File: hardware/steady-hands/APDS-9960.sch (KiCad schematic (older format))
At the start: 8 parts

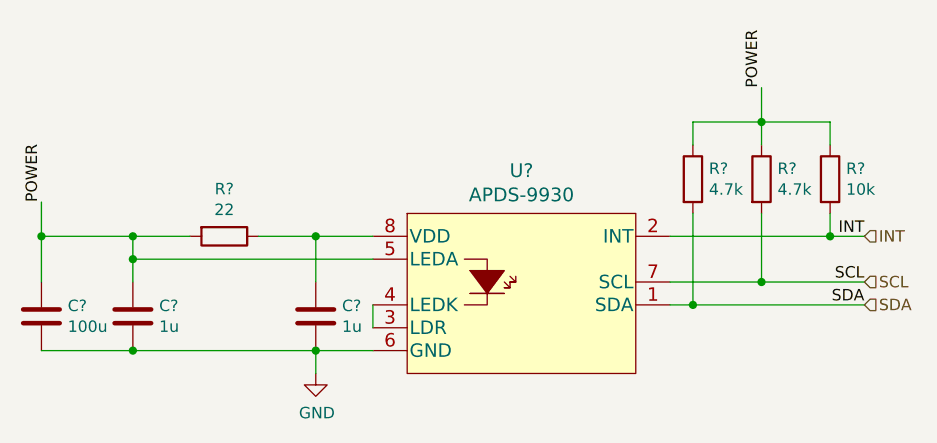
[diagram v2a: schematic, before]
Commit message: Completes schematic connections
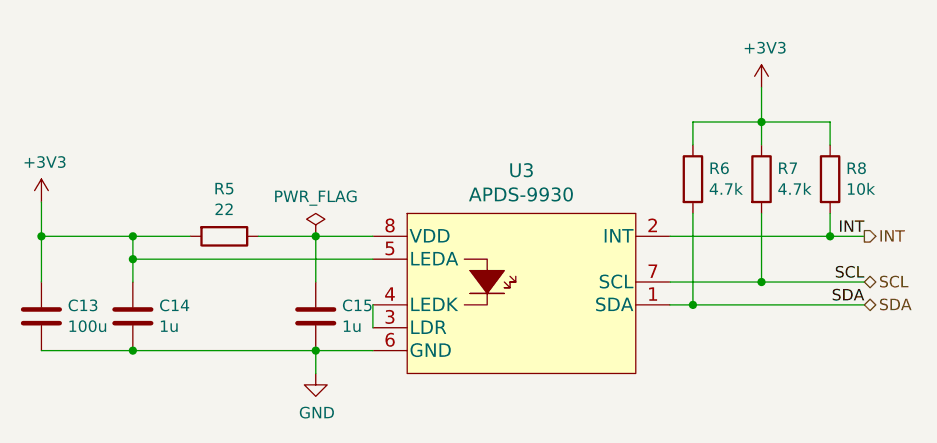
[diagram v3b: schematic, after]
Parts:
- gave numbers to parts that had none: 8
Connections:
- net POWER renamed +3V3
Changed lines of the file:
@@
 $Descr A4 11693 8268
 encoding utf-8
-Sheet 3 7
+Sheet 2 7
 Title ""
 Date ""
@@
 P 6050 3600
 AR Path="/5EF9057A" Ref="U?"  Part="1"
-AR Path="/5EF838FE/5EF9057A" Ref="U?"  Part="1"
-F 0 "U?" H 6050 3787 60  0000 C CNN
+AR Path="/5EF838FE/5EF9057A" Ref="U3"  Part="1"
+F 0 "U3" H 6050 3787 60  0000 C CNN
 F 1 "APDS-9930" H 6050 3681 60  0000 C CNN
 F 2 "QFN_DS-9930" H 6050 3600 60  0001 C CNN
@@
 P 4350 4050
 AR Path="/5EF90580" Ref="C?"  Part="1"
-AR Path="/5EF838FE/5EF90580" Ref="C?"  Part="1"
-F 0 "C?" H 4235 4004 50  0000 R CNN
+AR Path="/5EF838FE/5EF90580" Ref="C14"  Part="1"
+F 0 "C14" H 4235 4004 50  0000 R CNN
 F 1 "1u" H 4235 4095 50  0000 R CNN
 F 2 "" H 4388 3900 50  0001 C CNN
@@
 P 5150 4050
 AR Path="/5EF90586" Ref="C?"  Part="1"
-AR Path="/5EF838FE/5EF90586" Ref="C?"  Part="1"
-F 0 "C?" H 5035 4004 50  0000 R CNN
+AR Path="/5EF838FE/5EF90586" Ref="C15"  Part="1"
+F 0 "C15" H 5035 4004 50  0000 R CNN
 F 1 "1u" H 5035 4095 50  0000 R CNN
 F 2 "" H 5188 3900 50  0001 C CNN
@@
 P 5150 4300
 AR Path="/5EF9058C" Ref="#PWR?"  Part="1"
-AR Path="/5EF838FE/5EF9058C" Ref="#PWR?"  Part="1"
-F 0 "#PWR?" H 5150 4050 50  0001 C CNN
+AR Path="/5EF838FE/5EF9058C" Ref="#PWR0125"  Part="1"
+F 0 "#PWR0125" H 5150 4050 50  0001 C CNN
 F 1 "GND" H 5155 4127 50  0000 C CNN
 F 2 "" H 5150 4300 50  0001 C CNN
@@
 P 4750 3700
 AR Path="/5EF90592" Ref="R?"  Part="1"
-AR Path="/5EF838FE/5EF90592" Ref="R?"  Part="1"
-F 0 "R?" V 4543 3700 50  0000 C CNN
+AR Path="/5EF838FE/5EF90592" Ref="R5"  Part="1"
+F 0 "R5" V 4543 3700 50  0000 C CNN
 F 1 "22" V 4634 3700 50  0000 C CNN
 F 2 "" V 4680 3700 50  0001 C CNN
@@
 P 3950 4050
 AR Path="/5EF905A6" Ref="C?"  Part="1"
-AR Path="/5EF838FE/5EF905A6" Ref="C?"  Part="1"
-F 0 "C?" H 3835 4004 50  0000 R CNN
+AR Path="/5EF838FE/5EF905A6" Ref="C13"  Part="1"
+F 0 "C13" H 3835 4004 50  0000 R CNN
 F 1 "100u" H 3835 4095 50  0000 R CNN
 F 2 "" H 3988 3900 50  0001 C CNN
@@
 P 6800 3450
 AR Path="/5EF905AE" Ref="R?"  Part="1"
-AR Path="/5EF838FE/5EF905AE" Ref="R?"  Part="1"
-F 0 "R?" H 6870 3496 50  0000 L CNN
+AR Path="/5EF838FE/5EF905AE" Ref="R6"  Part="1"
+F 0 "R6" H 6870 3496 50  0000 L CNN
 F 1 "4.7k" H 6870 3405 50  0000 L CNN
 F 2 "" V 6730 3450 50  0001 C CNN
@@
 P 7100 3450
 AR Path="/5EF905B4" Ref="R?"  Part="1"
-AR Path="/5EF838FE/5EF905B4" Ref="R?"  Part="1"
-F 0 "R?" H 7170 3496 50  0000 L CNN
+AR Path="/5EF838FE/5EF905B4" Ref="R7"  Part="1"
+F 0 "R7" H 7170 3496 50  0000 L CNN
 F 1 "4.7k" H 7170 3405 50  0000 L CNN
 F 2 "" V 7030 3450 50  0001 C CNN
@@
 P 7400 3450
 AR Path="/5EF905BA" Ref="R?"  Part="1"
-AR Path="/5EF838FE/5EF905BA" Ref="R?"  Part="1"
-F 0 "R?" H 7470 3496 50  0000 L CNN
+AR Path="/5EF838FE/5EF905BA" Ref="R8"  Part="1"
+F 0 "R8" H 7470 3496 50  0000 L CNN
 F 1 "10k" H 7470 3405 50  0000 L CNN
 F 2 "" V 7330 3450 50  0001 C CNN
@@
 Wire Wire Line
 	3950 4200 4350 4200
-Text Label 3950 3550 1    50   ~ 0
-POWER
-Text Label 7100 3050 1    50   ~ 0
-POWER
 Text Label 7550 3700 2    50   ~ 0
 INT
@@
 Text Label 7550 4000 2    50   ~ 0
 SDA
-Text HLabel 7550 3700 2    50   Input ~ 0
+Text HLabel 7550 3700 2    50   Output ~ 0
 INT
-Text HLabel 7550 3900 2    50   Input ~ 0
+Text HLabel 7550 3900 2    50   BiDi ~ 0
 SCL
-Text HLabel 7550 4000 2    50   Input ~ 0
+Text HLabel 7550 4000 2    50   BiDi ~ 0
 SDA
+$Comp
+L power:+3V3 #PWR0164
+U 1 1 5F25AE43
+P 7100 3050
+F 0 "#PWR0164" H 7100 2900 50  0001 C CNN
+F 1 "+3V3" H 7115 3223 50  0000 C CNN
+F 2 "" H 7100 3050 50  0001 C CNN
+F 3 "" H 7100 3050 50  0001 C CNN
+	1    7100 3050
+	1    0    0    -1
+$EndComp
+$Comp
+L power:+3V3 #PWR0165
+U 1 1 5F25AF93
+P 3950 3550
+F 0 "#PWR0165" H 3950 3400 50  0001 C CNN
+F 1 "+3V3" H 3965 3723 50  0000 C CNN
+F 2 "" H 3950 3550 50  0001 C CNN
+F 3 "" H 3950 3550 50  0001 C CNN
+	1    3950 3550
+	1    0    0    -1
+$EndComp
+$Comp
+L power:PWR_FLAG #FLG0109
+U 1 1 5F25B62C
+P 5150 3700
+F 0 "#FLG0109" H 5150 3775 50  0001 C CNN
+F 1 "PWR_FLAG" H 5150 3873 50  0000 C CNN
+F 2 "" H 5150 3700 50  0001 C CNN
+F 3 "~" H 5150 3700 50  0001 C CNN
+	1    5150 3700
+	1    0    0    -1
+$EndComp
 $EndSCHEMATC

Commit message: Adds footprints
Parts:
- C13, C14, C15: footprint (none) -> Capacitor_SMD:C_0402_1005Metric
- R5, R6, R7, R8: footprint (none) -> Resistor_SMD:R_0402_1005Metric
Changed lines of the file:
@@
 F 0 "C14" H 4235 4004 50  0000 R CNN
 F 1 "1u" H 4235 4095 50  0000 R CNN
-F 2 "" H 4388 3900 50  0001 C CNN
+F 2 "Capacitor_SMD:C_0402_1005Metric" H 4388 3900 50  0001 C CNN
 F 3 "~" H 4350 4050 50  0001 C CNN
 	1    4350 4050
@@
 F 0 "C15" H 5035 4004 50  0000 R CNN
 F 1 "1u" H 5035 4095 50  0000 R CNN
-F 2 "" H 5188 3900 50  0001 C CNN
+F 2 "Capacitor_SMD:C_0402_1005Metric" H 5188 3900 50  0001 C CNN
 F 3 "~" H 5150 4050 50  0001 C CNN
 	1    5150 4050
@@
 F 0 "R5" V 4543 3700 50  0000 C CNN
 F 1 "22" V 4634 3700 50  0000 C CNN
-F 2 "" V 4680 3700 50  0001 C CNN
+F 2 "Resistor_SMD:R_0402_1005Metric" V 4680 3700 50  0001 C CNN
 F 3 "~" H 4750 3700 50  0001 C CNN
 	1    4750 3700
@@
 F 0 "C13" H 3835 4004 50  0000 R CNN
 F 1 "100u" H 3835 4095 50  0000 R CNN
-F 2 "" H 3988 3900 50  0001 C CNN
+F 2 "Capacitor_SMD:C_0402_1005Metric" H 3988 3900 50  0001 C CNN
 F 3 "~" H 3950 4050 50  0001 C CNN
 	1    3950 4050
@@
 F 0 "R6" H 6870 3496 50  0000 L CNN
 F 1 "4.7k" H 6870 3405 50  0000 L CNN
-F 2 "" V 6730 3450 50  0001 C CNN
+F 2 "Resistor_SMD:R_0402_1005Metric" V 6730 3450 50  0001 C CNN
 F 3 "~" H 6800 3450 50  0001 C CNN
 	1    6800 3450
@@
 F 0 "R7" H 7170 3496 50  0000 L CNN
 F 1 "4.7k" H 7170 3405 50  0000 L CNN
-F 2 "" V 7030 3450 50  0001 C CNN
+F 2 "Resistor_SMD:R_0402_1005Metric" V 7030 3450 50  0001 C CNN
 F 3 "~" H 7100 3450 50  0001 C CNN
 	1    7100 3450
@@
 F 0 "R8" H 7470 3496 50  0000 L CNN
 F 1 "10k" H 7470 3405 50  0000 L CNN
-F 2 "" V 7330 3450 50  0001 C CNN
+F 2 "Resistor_SMD:R_0402_1005Metric" V 7330 3450 50  0001 C CNN
 F 3 "~" H 7400 3450 50  0001 C CNN
 	1    7400 3450
